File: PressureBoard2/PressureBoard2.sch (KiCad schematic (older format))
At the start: 12 parts, among them J1 Jack-DC, J2 Conn_01x02_Male, SW1 TL2230OA, U1 ASDXACX030PAAA5

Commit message: Agrego segunda versión del esquemático que, incluye: power jack, switch DPDT de 6 y led indicador de encendido.
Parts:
- removed J1: Jack-DC, symbol Connector:Jack-DC
- removed RV1: 10K, symbol Device:R_POT_TRIM
- added C3: 470u, symbol Device:C
- added J1: POWER_JACK, POWER_JACK_PTH, symbol SparkFun-Connectors:POWER_JACK
- added R2, R4, R5: 10K, symbol Device:R
- U1: symbol ASDX:ASDXACX030PAAA5 -> PressureBoard2-rescue:ASDXACX030PAAA5-ASDX
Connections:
- net labels removed: GNDA
- wire segments 48 -> 62
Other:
- note added: "Filtro Antialiasing y salida de 5v a 3v3"
- moved on the sheet: J2, RV2
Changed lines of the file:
@@
 $EndComp
 $Comp
-L ASDX:ASDXACX030PAAA5 U1
+L PressureBoard2-rescue:ASDXACX030PAAA5-ASDX U1
 U 1 1 5C9C80E7
 P 2100 4550
@@
 $EndComp
 $Comp
-L Connector:Jack-DC J1
-U 1 1 5C9C8299
-P 1200 1300
-F 0 "J1" H 1255 1625 50  0000 C CNN
-F 1 "Jack-DC" H 1255 1534 50  0000 C CNN
-F 2 "" H 1250 1260 50  0001 C CNN
-F 3 "~" H 1250 1260 50  0001 C CNN
-	1    1200 1300
-	1    0    0    -1
-$EndComp
-$Comp
 L Device:R R1
 U 1 1 5C9C8396
@@
 $EndComp
 $Comp
-L Device:R_POT_TRIM RV1
-U 1 1 5C9C8507
+L Device:R_POT_TRIM RV2
+U 1 1 5C9C8599
 P 3700 1850
-F 0 "RV1" H 3630 1896 50  0000 R CNN
+F 0 "RV2" H 3630 1896 50  0000 R CNN
 F 1 "10K" H 3630 1805 50  0000 R CNN
 F 2 "" H 3700 1850 50  0001 C CNN
@@
 	1    0    0    -1
 $EndComp
-$Comp
-L Device:R_POT_TRIM RV2
-U 1 1 5C9C8599
-P 3700 2300
-F 0 "RV2" H 3630 2346 50  0000 R CNN
-F 1 "10K" H 3630 2255 50  0000 R CNN
-F 2 "" H 3700 2300 50  0001 C CNN
-F 3 "~" H 3700 2300 50  0001 C CNN
-	1    3700 2300
-	1    0    0    -1
-$EndComp
-Wire Wire Line
-	4300 1300 3700 1300
-Wire Wire Line
-	3700 1300 3700 1700
-Wire Wire Line
-	3500 1300 3700 1300
-Connection ~ 3700 1300
-Wire Wire Line
-	4200 1850 4050 1850
 Wire Wire Line
 	4300 1300 4300 1750
 Wire Wire Line
-	3700 2150 3700 2000
-Wire Wire Line
 	4300 1950 4300 2600
 Wire Wire Line
 	4300 2600 4000 2600
-Wire Wire Line
-	3700 2600 3700 2450
 Wire Wire Line
 	4300 1300 4700 1300
@@
 Wire Wire Line
 	4000 2600 3700 2600
-Wire Wire Line
-	4000 2600 4000 2700
-$Comp
-L power:GNDA #PWR04
-U 1 1 5C9C96AC
-P 2700 5250
-F 0 "#PWR04" H 2700 5000 50  0001 C CNN
-F 1 "GNDA" H 2705 5077 50  0000 C CNN
-F 2 "" H 2700 5250 50  0001 C CNN
-F 3 "" H 2700 5250 50  0001 C CNN
-	1    2700 5250
-	1    0    0    -1
-$EndComp
 $Comp
 L Device:C_Small C1
@@
 	2550 5050 2700 5050
 Wire Wire Line
-	2700 5250 2700 5050
-Wire Wire Line
 	2650 4300 2650 4200
 Wire Wire Line
@@
 Wire Wire Line
 	3050 3900 3050 4750
-Wire Wire Line
-	3850 2300 4050 2300
-Wire Wire Line
-	4050 2300 4050 1850
-Connection ~ 4050 1850
-Wire Wire Line
-	4050 1850 3850 1850
-$Comp
-L power:PWR_FLAG #FLG0101
-U 1 1 5C9CC1E8
-P 4700 2550
-F 0 "#FLG0101" H 4700 2625 50  0001 C CNN
-F 1 "PWR_FLAG" H 4700 2724 50  0000 C CNN
-F 2 "" H 4700 2550 50  0001 C CNN
-F 3 "~" H 4700 2550 50  0001 C CNN
-	1    4700 2550
-	1    0    0    -1
-$EndComp
-Wire Wire Line
-	4000 2700 4700 2700
-Wire Wire Line
-	4700 2700 4700 2550
-Connection ~ 4000 2700
-Wire Wire Line
-	4000 2700 4000 2750
 Wire Wire Line
 	3050 3900 3350 3900
@@
 Connection ~ 4700 1300
 $Comp
-L power:PWR_FLAG #FLG0103
-U 1 1 5C9CDA24
-P 3050 5250
-F 0 "#FLG0103" H 3050 5325 50  0001 C CNN
-F 1 "PWR_FLAG" H 3050 5423 50  0000 C CNN
-F 2 "" H 3050 5250 50  0001 C CNN
-F 3 "~" H 3050 5250 50  0001 C CNN
-	1    3050 5250
-	-1   0    0    1
-$EndComp
-Wire Wire Line
-	2700 5050 3050 5050
-Wire Wire Line
-	3050 5050 3050 5250
-Connection ~ 2700 5050
-$Comp
 L Connector:Conn_01x02_Male J2
 U 1 1 5C9CE6EF
-P 3400 4900
-F 0 "J2" H 3373 4873 50  0000 R CNN
-F 1 "Conn_01x02_Male" H 3373 4782 50  0000 R CNN
-F 2 "" H 3400 4900 50  0001 C CNN
-F 3 "~" H 3400 4900 50  0001 C CNN
-	1    3400 4900
+P 5300 4750
+F 0 "J2" H 5273 4723 50  0000 R CNN
+F 1 "Conn_01x02_Male" H 5273 4632 50  0000 R CNN
+F 2 "" H 5300 4750 50  0001 C CNN
+F 3 "~" H 5300 4750 50  0001 C CNN
+	1    5300 4750
 	-1   0    0    -1
 $EndComp
-Wire Wire Line
-	2550 4900 3200 4900
-Wire Wire Line
-	3200 5000 3050 5000
-Wire Wire Line
-	3050 5000 3050 5050
-Connection ~ 3050 5050
-Text Label 2600 4900 0    50   ~ 0
-Vout(ToTivaADC)
-Text Label 2600 5050 0    50   ~ 0
+Text Label 5000 5300 1    50   ~ 0
 GND(ToTiva)
 Wire Notes Line
-	1350 3400 4400 3400
-Wire Notes Line
-	4400 3400 4400 5750
-Wire Notes Line
-	4400 5750 1350 5750
-Wire Notes Line
 	1350 5750 1350 3400
-Wire Wire Line
-	1500 1400 1750 1400
 Wire Wire Line
 	1750 1400 1750 1550
@@
 	1    0    0    -1
 $EndComp
-Wire Wire Line
-	1500 1200 2000 1200
 Connection ~ 2000 1200
 Wire Wire Line
@@
 	3000 1850 3000 2100
 Wire Wire Line
-	3000 2450 3000 2300
-Wire Wire Line
 	2000 1750 2150 1750
 Wire Wire Line
@@
 Wire Wire Line
 	3200 1300 2550 1300
+$Comp
+L SparkFun-Connectors:POWER_JACK J1
+U 1 1 5CA927BA
+P 1150 1300
+F 0 "J1" H 1106 1690 45  0000 C CNN
+F 1 "POWER_JACK" H 1106 1606 45  0000 C CNN
+F 2 "POWER_JACK_PTH" H 1150 1550 20  0001 C CNN
+F 3 "" H 1150 1300 50  0001 C CNN
+F 4 "CONN-08197" H 1106 1511 60  0000 C CNN "Field4"
+	1    1150 1300
+	1    0    0    -1
+$EndComp
+Wire Wire Line
+	1350 1200 2000 1200
+Wire Wire Line
+	1350 1300 1500 1300
+Wire Wire Line
+	1500 1300 1500 1400
+Wire Wire Line
+	1350 1400 1500 1400
+Connection ~ 1500 1400
+$Comp
+L Device:C C3
+U 1 1 5CA975BC
+P 4250 4750
+F 0 "C3" H 4365 4796 50  0000 L CNN
+F 1 "470u" H 4365 4705 50  0000 L CNN
+F 2 "" H 4288 4600 50  0001 C CNN
+F 3 "~" H 4250 4750 50  0001 C CNN
+	1    4250 4750
+	1    0    0    -1
+$EndComp
+Wire Wire Line
+	3500 1300 3700 1300
+Wire Wire Line
+	3700 1700 3700 1300
+Connection ~ 3700 1300
+Wire Wire Line
+	3700 1300 4300 1300
+Wire Wire Line
+	3700 2000 3700 2600
+Wire Wire Line
+	3850 1850 4200 1850
+$Comp
+L Device:R R4
+U 1 1 5CA9B431
+P 4650 4650
+F 0 "R4" V 4443 4650 50  0000 C CNN
+F 1 "10K" V 4534 4650 50  0000 C CNN
+F 2 "" V 4580 4650 50  0001 C CNN
+F 3 "~" H 4650 4650 50  0001 C CNN
+	1    4650 4650
+	-1   0    0    1
+$EndComp
+$Comp
+L Device:R R2
+U 1 1 5CA9BFB7
+P 3850 4300
+F 0 "R2" V 3643 4300 50  0000 C CNN
+F 1 "10K" V 3734 4300 50  0000 C CNN
+F 2 "" V 3780 4300 50  0001 C CNN
+F 3 "~" H 3850 4300 50  0001 C CNN
+	1    3850 4300
+	0    1    1    0
+$EndComp
+$Comp
+L Device:R R5
+U 1 1 5CA9C140
+P 4650 5050
+F 0 "R5" V 4443 5050 50  0000 C CNN
+F 1 "10K" V 4534 5050 50  0000 C CNN
+F 2 "" V 4580 5050 50  0001 C CNN
+F 3 "~" H 4650 5050 50  0001 C CNN
+	1    4650 5050
+	-1   0    0    1
+$EndComp
+$Comp
+L power:GND #PWR04
+U 1 1 5CA9C1D7
+P 2700 5250
+F 0 "#PWR04" H 2700 5000 50  0001 C CNN
+F 1 "GND" H 2705 5077 50  0000 C CNN
+F 2 "" H 2700 5250 50  0001 C CNN
+F 3 "" H 2700 5250 50  0001 C CNN
+	1    2700 5250
+	1    0    0    -1
+$EndComp
+$Comp
+L power:GND #PWR08
+U 1 1 5CA9C212
+P 4250 5350
+F 0 "#PWR08" H 4250 5100 50  0001 C CNN
+F 1 "GND" H 4255 5177 50  0000 C CNN
+F 2 "" H 4250 5350 50  0001 C CNN
+F 3 "" H 4250 5350 50  0001 C CNN
+	1    4250 5350
+	1    0    0    -1
+$EndComp
+Wire Wire Line
+	4250 4900 4250 5300
+Wire Wire Line
+	4000 4300 4250 4300
+Wire Wire Line
+	4250 4300 4250 4600
+Wire Wire Line
+	4650 4900 4650 4800
+Wire Wire Line
+	4250 5300 4650 5300
+Wire Wire Line
+	4650 5300 4650 5200
+Connection ~ 4250 5300
+Wire Wire Line
+	4250 5300 4250 5350
+Wire Wire Line
+	4650 4500 4650 4300
+Wire Wire Line
+	4650 4300 4250 4300
+Connection ~ 4250 4300
+Text Label 5000 4750 1    50   ~ 0
+Vout(ToTivaADC)
+Wire Wire Line
+	4000 2600 4000 2750
+Wire Wire Line
+	5100 4750 5000 4750
+Wire Wire Line
+	5000 4750 5000 4300
+Wire Wire Line
+	5000 4300 4650 4300
+Connection ~ 4650 4300
+Wire Wire Line
+	5100 4850 5000 4850
+Wire Wire Line
+	5000 4850 5000 5300
+Wire Wire Line
+	5000 5300 4650 5300
+Connection ~ 4650 5300
+Wire Wire Line
+	2700 5050 2700 5250
+Wire Wire Line
+	1500 1400 1750 1400
+Wire Wire Line
+	3000 2300 3000 2450
+$Comp
+L power:PWR_FLAG #FLG0101
+U 1 1 5CAB78ED
+P 4550 2400
+F 0 "#FLG0101" H 4550 2475 50  0001 C CNN
+F 1 "PWR_FLAG" H 4550 2574 50  0000 C CNN
+F 2 "" H 4550 2400 50  0001 C CNN
+F 3 "~" H 4550 2400 50  0001 C CNN
+	1    4550 2400
+	1    0    0    -1
+$EndComp
+Wire Wire Line
+	4550 2400 4550 2600
+Wire Wire Line
+	4550 2600 4300 2600
+Connection ~ 4300 2600
+Wire Wire Line
+	2550 4900 3550 4900
+Wire Wire Line
+	3550 4900 3550 4300
+Wire Wire Line
+	3550 4300 3700 4300
+Wire Wire Line
+	4250 5300 3550 5300
+Wire Wire Line
+	3550 5300 3550 5050
+Wire Wire Line
+	3550 5050 2700 5050
+Connection ~ 2700 5050
+Wire Notes Line
+	6200 3400 6200 5750
+Wire Notes Line
+	1350 3400 6200 3400
+Wire Notes Line
+	1350 5750 6200 5750
+Text Notes 4150 4150 0    50   ~ 0
+Filtro Antialiasing y salida de 5v a 3v3
 $EndSCHEMATC

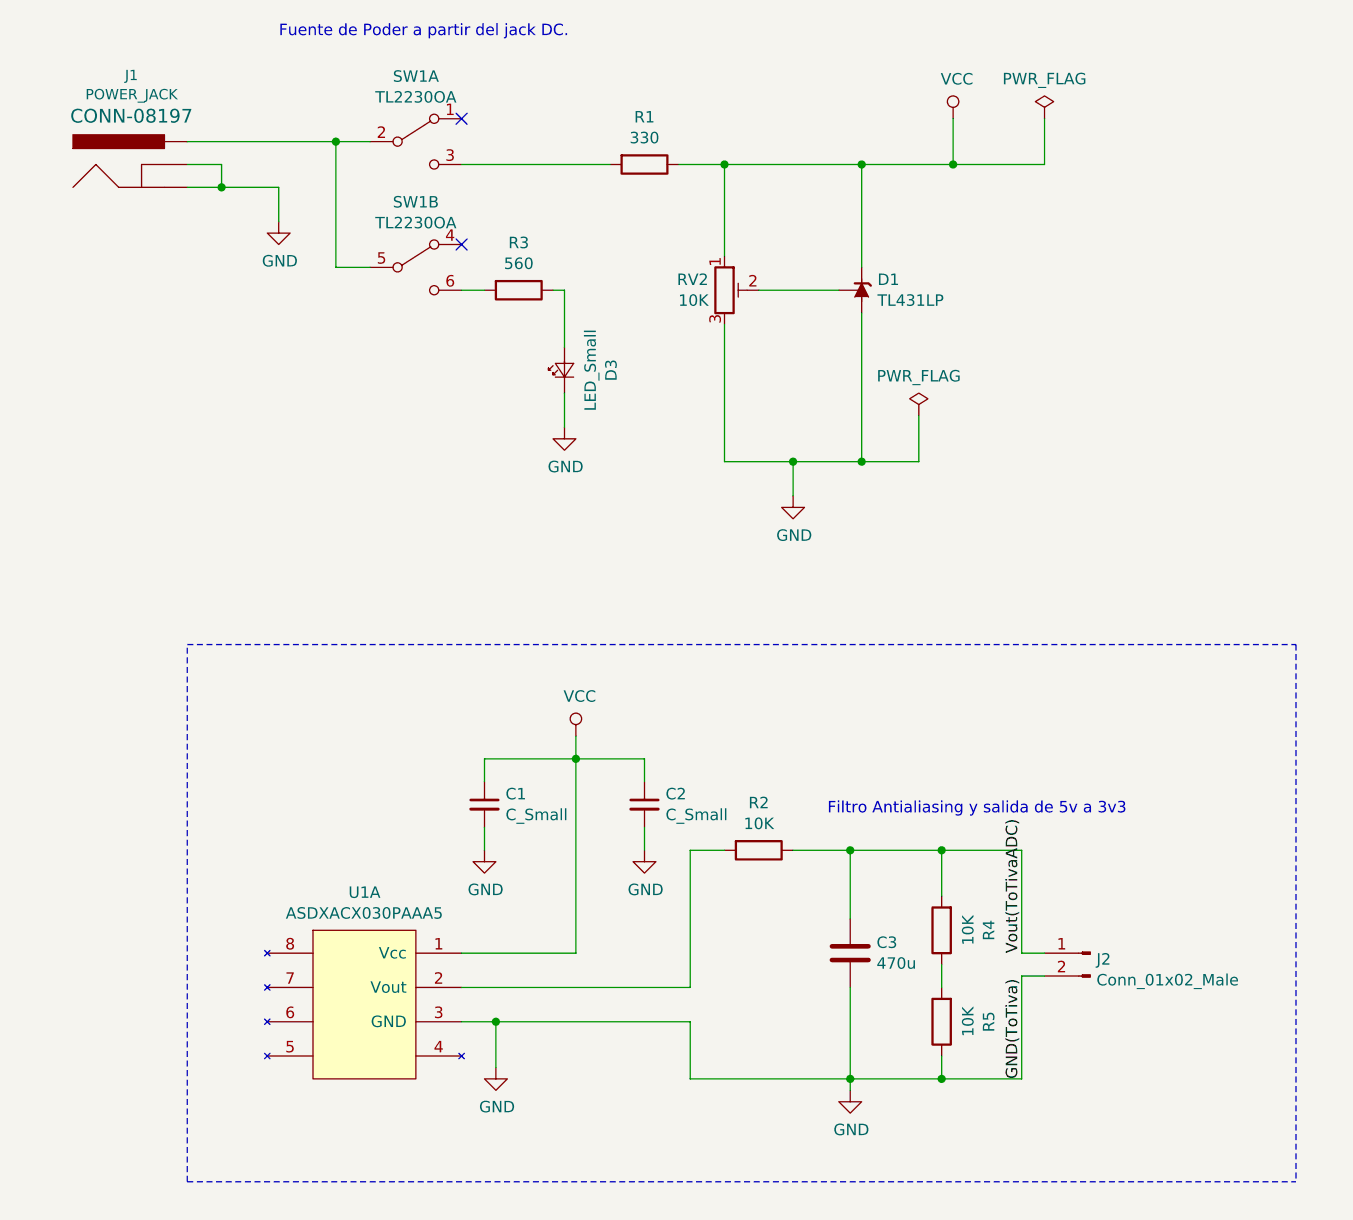
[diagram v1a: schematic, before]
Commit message: Agrego versión 3: Creación de footprint para ASDXACX030PAAA5, netlist de componentes y esquemático
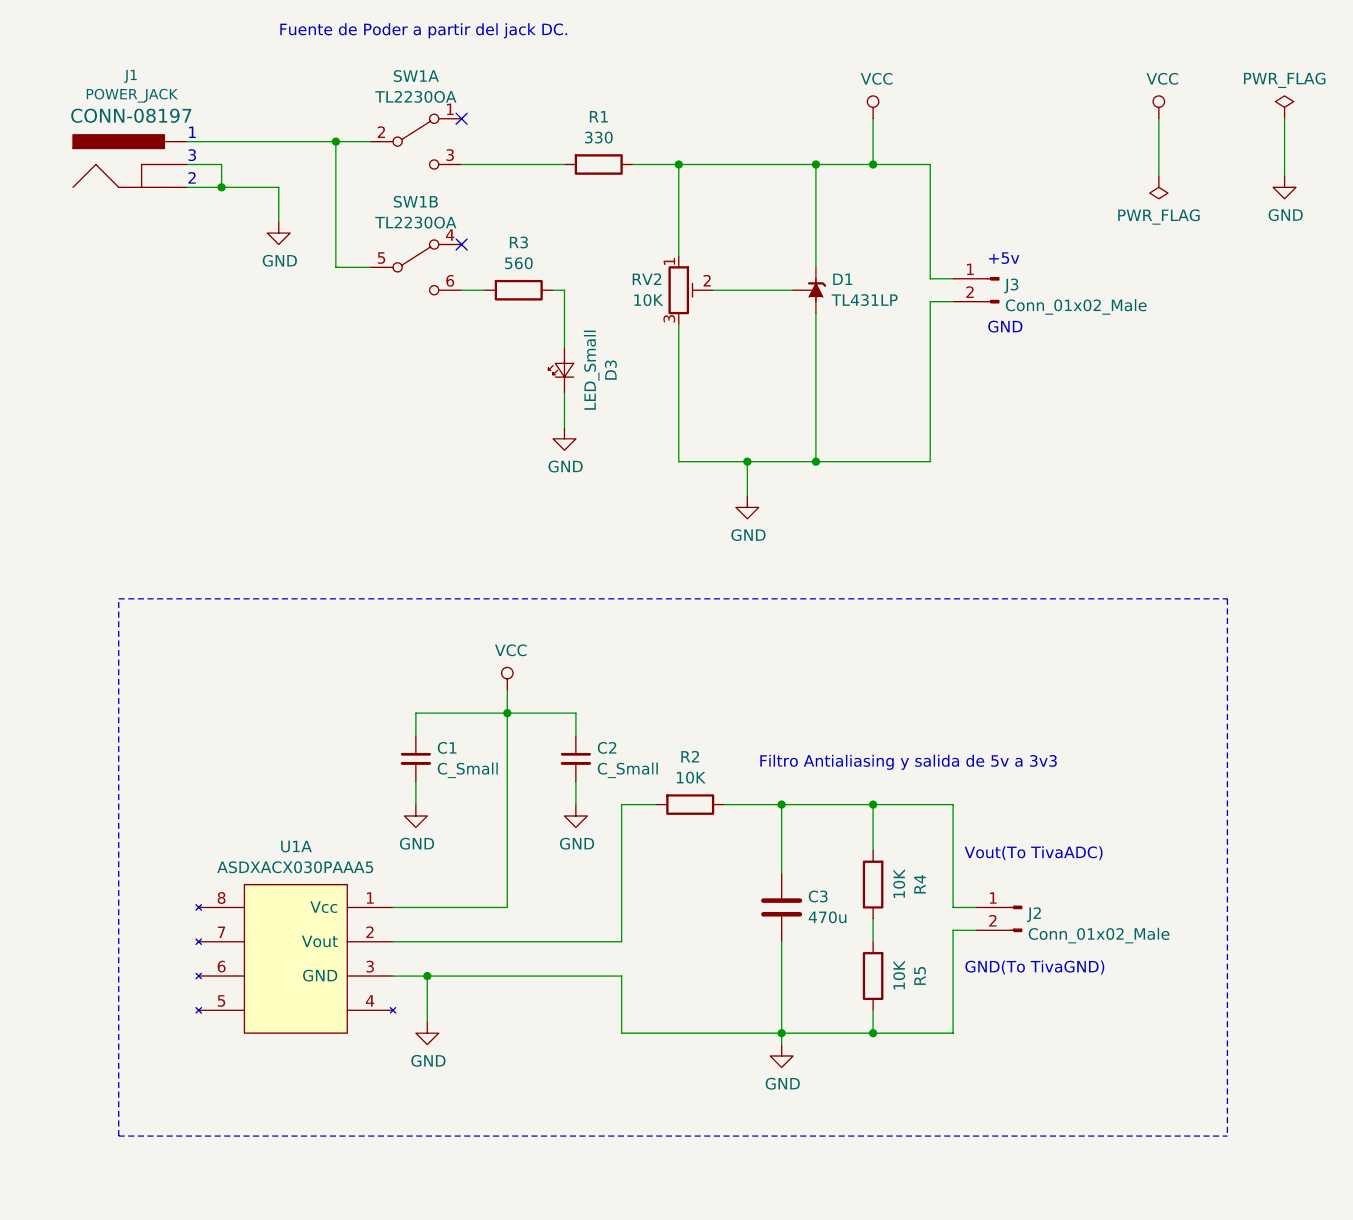
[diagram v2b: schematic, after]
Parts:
- added J3: Conn_01x02_Male, Footprints:PinHeader_1x02_P2.54mm_Vertical, symbol Connector:Conn_01x02_Male
- C1, C2: footprint (none) -> Footprints:C_Disc_D3.0mm_W1.6mm_P2.50mm
- C3: footprint (none) -> Footprints:C_Disc_D10.5mm_W5.0mm_P7.50mm; Digikey# (none) -> BFC236825474-ND; Manf (none) -> Vishay / BC Components; Manf# (none) -> BFC236825474; Mouser# (none) -> 594-2222-368-25474
- D1: footprint Package_TO_SOT_THT:TO-92_Inline -> Footprints:TO-92_Inline; Digikey# (none) -> 296-1290-2-ND; Manf (none) -> Texas Instruments; Manf# (none) -> TL431CLPR; Mouser# (none) -> 595-TL431CLPR
- D3: footprint (none) -> Footprints:LED_D2.0mm_W4.8mm_H2.5mm_FlatTop
- J1: footprint POWER_JACK_PTH -> Footprints:BarrelJack_Horizontal; Digikey# (none) -> CP-202A-ND; Manf (none) -> CUI Inc.; Manf# (none) -> PJ-202A; Mouser# (none) -> 490-PJ-202A
- J2: footprint (none) -> Footprints:PinHeader_1x02_P2.54mm_Vertical
- R1, R2, R3, R4, R5: footprint (none) -> Footprints:Resistor_Horizontal_RM10mm
- RV2: footprint (none) -> Footprints:Potentiometer_Bourns_3296W_Vertical
- SW1: footprint e-switch:TL2230 -> Footprints:TL2230; Manf (none) -> CW Industries; Manf# (none) -> GPBS-800L; Mouser# (none) -> 629-GPBS-800L
- SW1: footprint e-switch:TL2230 -> Footprints:TL2230; Digikey# (none) -> CW177-ND; Manf (none) -> CW Industries; Manf# (none) -> GPBS-800L; Mouser# (none) -> 629-GPBS-800L
- U1: footprint (none) -> Footprints:ASDXACX030PAAA5
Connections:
- net GND: now also J3.2 (Pin_2)
- net VCC: now also J3.1 (Pin_1)
- net Vout(ToTivaADC): no longer names the net of C3.1, J2.1 (Pin_1), R2.1, R4.2
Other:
- note added: "+5v"
- note added: "1"
- note added: "2"
- note added: "3"
- note added: "GND"
- note added: "GND(To TivaGND)"
- note added: "Vout(To TivaADC)"
- moved on the sheet: C1, C2, C3, D1, J2, R1, R2, R4, R5, RV2, U1A

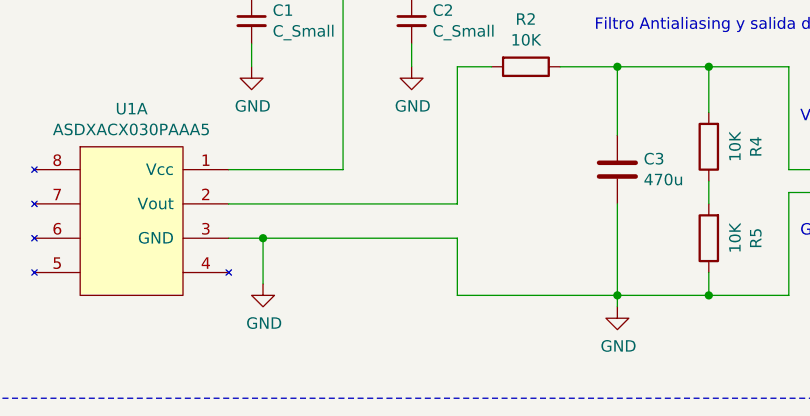
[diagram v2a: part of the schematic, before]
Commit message: AGrego modificaciones en las dimesniones del sensor ASDX , en el netlist y la asignadión de footprints en el cvPCB.
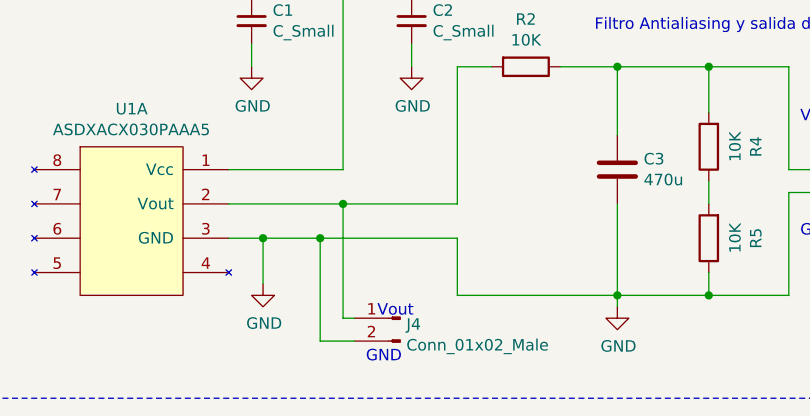
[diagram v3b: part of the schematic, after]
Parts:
- added J4: Conn_01x02_Male, Footprints:PinHeader_1x02_P2.54mm_Vertical, symbol Connector:Conn_01x02_Male
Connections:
- net GND: now also J4.2 (Pin_2)
- net at R2.2, U1.2 (Vout): now also J4.1 (Pin_1)
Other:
- note added: "Vout"
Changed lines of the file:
@@
 	3000 2300 3000 2450
 Wire Wire Line
-	2250 4700 3250 4700
+	2250 4700 2750 4700
 Wire Wire Line
 	3250 4700 3250 4100
@@
 	3250 5100 3250 4850
 Wire Wire Line
-	3250 4850 2400 4850
+	3250 4850 2650 4850
 Connection ~ 2400 4850
 Wire Notes Line
@@
 Wire Wire Line
 	2550 1300 3000 1300
+$Comp
+L Connector:Conn_01x02_Male J4
+U 1 1 5CAC3E58
+P 3000 5200
+F 0 "J4" H 2973 5173 50  0000 R CNN
+F 1 "Conn_01x02_Male" H 2973 5082 50  0000 R CNN
+F 2 "Footprints:PinHeader_1x02_P2.54mm_Vertical" H 3000 5200 50  0001 C CNN
+F 3 "~" H 3000 5200 50  0001 C CNN
+	1    3000 5200
+	-1   0    0    -1
+$EndComp
+Wire Wire Line
+	2800 5200 2750 5200
+Wire Wire Line
+	2750 5200 2750 4700
+Connection ~ 2750 4700
+Wire Wire Line
+	2750 4700 3250 4700
+Wire Wire Line
+	2800 5300 2650 5300
+Wire Wire Line
+	2650 5300 2650 4850
+Connection ~ 2650 4850
+Wire Wire Line
+	2650 4850 2400 4850
+Text Notes 2900 5200 0    50   ~ 0
+Vout
+Text Notes 2850 5400 0    50   ~ 0
+GND
 $EndSCHEMATC

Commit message: PCVBV1
Agrego versión de PCB con ruteo y llenado de zonas de cobre.
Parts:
- removed J1: POWER_JACK, Footprints:BarrelJack_Horizontal, symbol SparkFun-Connectors:POWER_JACK
- added J1: Barrel_Jack_Switch, Footprints:BarrelJack_Horizontal, symbol Connector:Barrel_Jack_Switch
- R3: value 560 -> 1k
- SW1: symbol e-switch:TL2230OA -> PressureBoard2-rescue:TL2230OA-e-switch
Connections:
- net GND: now also J1.2, J1.3
- net at SW1.2 (B), SW1.5 (B): now also J1.1
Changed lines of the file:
@@
 EESchema Schematic File Version 4
 LIBS:PressureBoard2-cache
-EELAYER 26 0
+EELAYER 29 0
 EELAYER END
 $Descr A4 11693 8268
@@
 	1750 1400 1750 1550
 $Comp
-L e-switch:TL2230OA SW1
+L PressureBoard2-rescue:TL2230OA-e-switch SW1
 U 2 1 5CA7F2AF
 P 2350 1750
@@
 P 2800 1850
 F 0 "R3" V 2593 1850 50  0000 C CNN
-F 1 "560" V 2684 1850 50  0000 C CNN
+F 1 "1k" V 2684 1850 50  0000 C CNN
 F 2 "Footprints:Resistor_Horizontal_RM10mm" V 2730 1850 50  0001 C CNN
 F 3 "~" H 2800 1850 50  0001 C CNN
@@
 	2000 1200 2000 1750
 $Comp
-L e-switch:TL2230OA SW1
+L PressureBoard2-rescue:TL2230OA-e-switch SW1
 U 1 1 5CA7F223
 P 2350 1200
@@
 Text Notes 1750 750  0    50   ~ 0
 Fuente de Poder a partir del jack DC.
-$Comp
-L SparkFun-Connectors:POWER_JACK J1
-U 1 1 5CA927BA
-P 1150 1300
-F 0 "J1" H 1106 1690 45  0000 C CNN
-F 1 "POWER_JACK" H 1106 1606 45  0000 C CNN
-F 2 "Footprints:BarrelJack_Horizontal" H 1150 1550 20  0001 C CNN
-F 3 "" H 1150 1300 50  0001 C CNN
-F 4 " CP-202A-ND " H 1150 1300 50  0001 C CNN "Digikey#"
-F 5 "CUI Inc." H 1150 1300 50  0001 C CNN "Manf"
-F 6 "PJ-202A " H 1150 1300 50  0001 C CNN "Manf#"
-F 7 "490-PJ-202A " H 1150 1300 50  0001 C CNN "Mouser#"
-F 8 "CONN-08197" H 1106 1511 60  0000 C CNN "Field4"
-	1    1150 1300
-	1    0    0    -1
-$EndComp
 Wire Wire Line
 	1350 1200 2000 1200
@@
 Text Notes 2850 5400 0    50   ~ 0
 GND
+$Comp
+L Connector:Barrel_Jack_Switch J1
+U 1 1 5CADB583
+P 1050 1300
+F 0 "J1" H 1107 1617 50  0000 C CNN
+F 1 "Barrel_Jack_Switch" H 1107 1526 50  0000 C CNN
+F 2 "Footprints:BarrelJack_Horizontal" H 1100 1260 50  0001 C CNN
+F 3 "~" H 1100 1260 50  0001 C CNN
+	1    1050 1300
+	1    0    0    -1
+$EndComp
 $EndSCHEMATC
